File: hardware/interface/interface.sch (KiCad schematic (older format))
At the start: 14 parts, among them IC1 ARDUINO NANO, J8 CONN_01X02, Q1 BC547

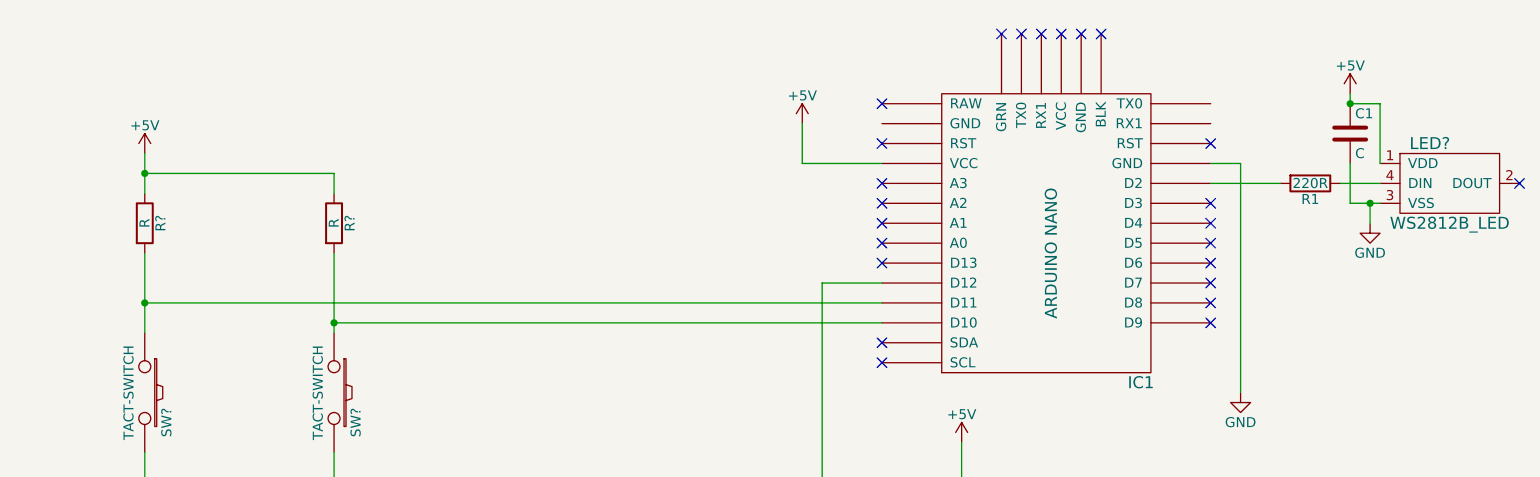
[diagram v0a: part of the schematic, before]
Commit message: Update diagram with LCD instead of LED.
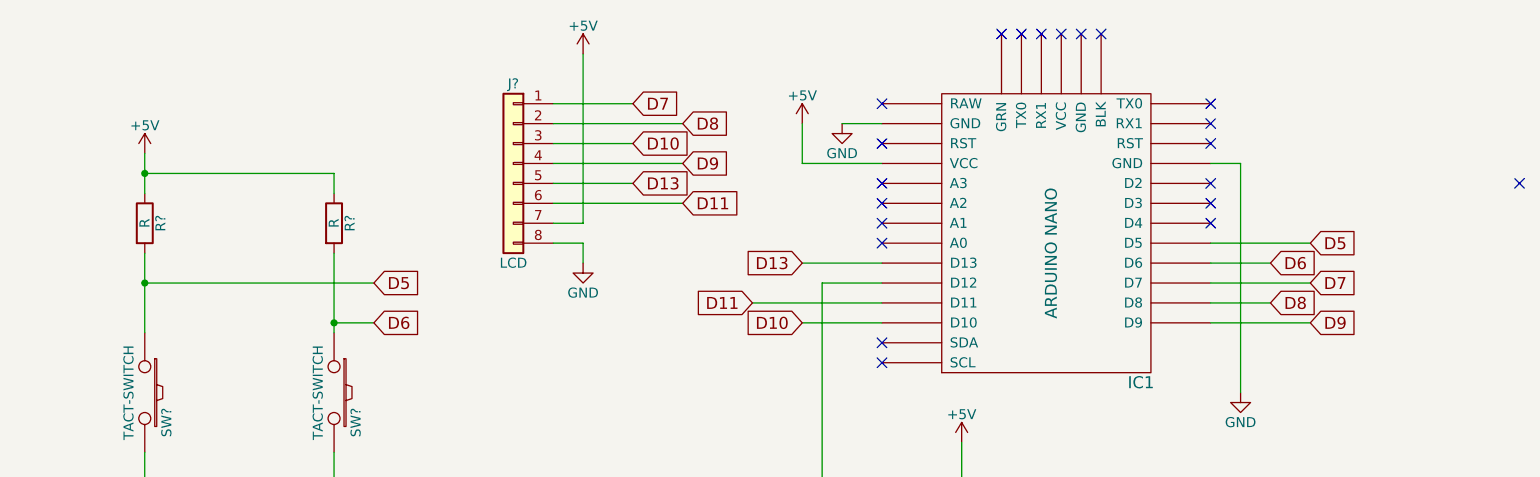
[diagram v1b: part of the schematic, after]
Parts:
- removed C1: C, symbol C
- removed LED?: WS2812B_LED, symbol WS2812B_LED
- removed R1: 220R, symbol R
- added J?: LCD, symbol Conn_01x08
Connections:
- net +5V: now also J?.7 (Pin_7)
- net GND: now also J?.8 (Pin_8)
- net D5: now reaches IC1.~ (VCC), R?.2, SW?.1
- net D6: now reaches IC1.~ (VCC), R?.2, SW?.1
- new net D10: IC1.~ (VCC), J?.3 (Pin_3)
- new net D11: IC1.~ (VCC), J?.6 (Pin_6)
- new net D13: IC1.~ (VCC), J?.5 (Pin_5)
- new net D7: IC1.~ (VCC), J?.1 (Pin_1)
- new net D8: IC1.~ (VCC), J?.2 (Pin_2)
- new net D9: IC1.~ (VCC), J?.4 (Pin_4)
- no-connect marks 24 -> 21
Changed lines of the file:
@@
 	1    0    0    -1
 $EndComp
-NoConn ~ 6650 2650
 $Comp
 L BC547 Q1
@@
 Wire Wire Line
 	1400 6350 1400 6550
-$Comp
-L WS2812B_LED LED?
-U 1 1 59806E4F
-P 9500 2250
-F 0 "LED?" H 9400 2450 60  0000 C CNN
-F 1 "WS2812B_LED" H 9500 2050 60  0000 C CNN
-F 2 "" H 9500 2250 60  0000 C CNN
-F 3 "" H 9500 2250 60  0000 C CNN
-	1    9500 2250
-	1    0    0    -1
-$EndComp
 NoConn ~ 9850 2250
-$Comp
-L R R1
-U 1 1 59806F2F
-P 8800 2250
-F 0 "R1" V 8880 2250 50  0000 C CNN
-F 1 "220R" V 8800 2250 50  0000 C CNN
-F 2 "" V 8730 2250 50  0001 C CNN
-F 3 "" H 8800 2250 50  0001 C CNN
-	1    8800 2250
-	0    1    1    0
-$EndComp
-Wire Wire Line
-	8300 2250 8650 2250
-Wire Wire Line
-	8950 2250 9150 2250
-$Comp
-L GND #PWR?
-U 1 1 59806FA3
-P 9100 2450
-F 0 "#PWR?" H 9100 2200 50  0001 C CNN
-F 1 "GND" H 9100 2300 50  0000 C CNN
-F 2 "" H 9100 2450 50  0001 C CNN
-F 3 "" H 9100 2450 50  0001 C CNN
-	1    9100 2450
-	1    0    0    -1
-$EndComp
-Wire Wire Line
-	9000 2350 9150 2350
-Wire Wire Line
-	9100 2350 9100 2450
-$Comp
-L +5V #PWR?
-U 1 1 59806FEE
-P 9000 1800
-F 0 "#PWR?" H 9000 1650 50  0001 C CNN
-F 1 "+5V" H 9000 1940 50  0000 C CNN
-F 2 "" H 9000 1800 50  0001 C CNN
-F 3 "" H 9000 1800 50  0001 C CNN
-	1    9000 1800
-	1    0    0    -1
-$EndComp
-$Comp
-L C C1
-U 1 1 59807012
-P 9000 2000
-F 0 "C1" H 9025 2100 50  0000 L CNN
-F 1 "C" H 9025 1900 50  0000 L CNN
-F 2 "" H 9038 1850 50  0001 C CNN
-F 3 "" H 9000 2000 50  0001 C CNN
-	1    9000 2000
-	1    0    0    -1
-$EndComp
-Wire Wire Line
-	9000 2150 9000 2350
-Connection ~ 9100 2350
-Wire Wire Line
-	9000 1800 9000 1850
-Wire Wire Line
-	9000 1850 9150 1850
-Wire Wire Line
-	9150 1850 9150 2150
-Connection ~ 9000 1850
 $Comp
 L TACT-SWITCH SW?
@@
 	3900 2200 3900 2300
 Connection ~ 2950 2200
-Wire Wire Line
-	6650 2850 2950 2850
-Connection ~ 2950 2850
-Wire Wire Line
-	6650 2950 3900 2950
+Connection ~ 2950 2750
 Connection ~ 3900 2950
 NoConn ~ 6650 3050
 NoConn ~ 6650 3150
+NoConn ~ 6650 2250
+NoConn ~ 6650 2350
+NoConn ~ 6650 2450
+NoConn ~ 6650 2550
+NoConn ~ 8300 2450
+NoConn ~ 8300 2350
+$Comp
+L GND #PWR?
+U 1 1 59807976
+P 8450 3300
+F 0 "#PWR?" H 8450 3050 50  0001 C CNN
+F 1 "GND" H 8450 3150 50  0000 C CNN
+F 2 "" H 8450 3300 50  0001 C CNN
+F 3 "" H 8450 3300 50  0001 C CNN
+	1    8450 3300
+	1    0    0    -1
+$EndComp
+$Comp
+L +5V #PWR?
+U 1 1 598079E4
+P 6250 1950
+F 0 "#PWR?" H 6250 1800 50  0001 C CNN
+F 1 "+5V" H 6250 2090 50  0000 C CNN
+F 2 "" H 6250 1950 50  0001 C CNN
+F 3 "" H 6250 1950 50  0001 C CNN
+	1    6250 1950
+	1    0    0    -1
+$EndComp
+Wire Wire Line
+	6250 1950 6250 2150
+Wire Wire Line
+	6250 2150 6650 2150
+Wire Wire Line
+	6650 4000 7600 4000
+$Comp
+L C C2
+U 1 1 59807C8B
+P 6650 4350
+F 0 "C2" H 6675 4450 50  0000 L CNN
+F 1 "100u" H 6675 4250 50  0000 L CNN
+F 2 "" H 6688 4200 50  0001 C CNN
+F 3 "" H 6650 4350 50  0001 C CNN
+	1    6650 4350
+	1    0    0    -1
+$EndComp
+Wire Wire Line
+	6650 4000 6650 4200
+Wire Wire Line
+	6650 4500 6650 5250
+Wire Wire Line
+	6650 5250 7600 5250
+Connection ~ 7600 5250
+$Comp
+L Conn_01x08 J?
+U 1 1 5A3D63D6
+P 4800 2150
+F 0 "J?" H 4800 2550 50  0000 C CNN
+F 1 "LCD" H 4800 1650 50  0000 C CNN
+F 2 "" H 4800 2150 50  0001 C CNN
+F 3 "" H 4800 2150 50  0001 C CNN
+	1    4800 2150
+	-1   0    0    -1
+$EndComp
+$Comp
+L GND #PWR?
+U 1 1 5A3D6483
+P 5150 2650
+F 0 "#PWR?" H 5150 2400 50  0001 C CNN
+F 1 "GND" H 5150 2500 50  0000 C CNN
+F 2 "" H 5150 2650 50  0001 C CNN
+F 3 "" H 5150 2650 50  0001 C CNN
+	1    5150 2650
+	1    0    0    -1
+$EndComp
+Wire Wire Line
+	5000 2550 5150 2550
+Wire Wire Line
+	5150 2550 5150 2650
+$Comp
+L +5V #PWR?
+U 1 1 5A3D64FD
+P 5150 1600
+F 0 "#PWR?" H 5150 1450 50  0001 C CNN
+F 1 "+5V" H 5150 1740 50  0000 C CNN
+F 2 "" H 5150 1600 50  0001 C CNN
+F 3 "" H 5150 1600 50  0001 C CNN
+	1    5150 1600
+	1    0    0    -1
+$EndComp
+Wire Wire Line
+	5150 1600 5150 2450
+Wire Wire Line
+	5150 2450 5000 2450
+Text GLabel 5650 1950 2    60   Input ~ 0
+D8
+Wire Wire Line
+	5400 1850 5000 1850
+Text GLabel 5400 2050 2    60   Input ~ 0
+D10
+Wire Wire Line
+	5650 1950 5000 1950
+Wire Wire Line
+	5400 2050 5000 2050
+Text GLabel 5650 2150 2    60   Input ~ 0
+D9
+Wire Wire Line
+	5650 2150 5000 2150
+Text GLabel 5400 2250 2    60   Input ~ 0
+D13
+Wire Wire Line
+	5400 2250 5000 2250
+Text GLabel 5650 2350 2    60   Input ~ 0
+D11
+Wire Wire Line
+	5650 2350 5000 2350
+Text GLabel 8600 2850 2    60   Input ~ 0
+D8
+Text GLabel 8800 2950 2    60   Input ~ 0
+D9
+Text GLabel 6000 2850 0    60   Input ~ 0
+D11
+Text GLabel 6250 2950 0    60   Input ~ 0
+D10
+Wire Wire Line
+	6250 2950 6650 2950
+Wire Wire Line
+	6650 2850 6000 2850
+Text GLabel 6250 2650 0    60   Input ~ 0
+D13
+Wire Wire Line
+	6250 2650 6650 2650
+Wire Wire Line
+	8300 2950 8800 2950
+Wire Wire Line
+	8600 2850 8300 2850
+Text GLabel 8800 2750 2    60   Input ~ 0
+D7
+Wire Wire Line
+	8300 2750 8800 2750
+Text GLabel 5400 1850 2    60   Input ~ 0
+D7
 $Comp
 L ARDUINO_PRO_MINI_5V IC1
@@
 	1    0    0    1
 $EndComp
-NoConn ~ 6650 2250
-NoConn ~ 6650 2350
-NoConn ~ 6650 2450
-NoConn ~ 6650 2550
-NoConn ~ 8300 2750
-NoConn ~ 8300 2650
-NoConn ~ 8300 2550
-NoConn ~ 8300 2450
-NoConn ~ 8300 2350
-NoConn ~ 8300 2850
-NoConn ~ 8300 2950
+Text GLabel 8600 2650 2    60   Input ~ 0
+D6
+Text GLabel 8800 2550 2    60   Input ~ 0
+D5
+Wire Wire Line
+	8800 2550 8300 2550
+Wire Wire Line
+	8300 2650 8600 2650
+Text GLabel 4100 2750 2    60   Input ~ 0
+D5
+Text GLabel 4100 2950 2    60   Input ~ 0
+D6
+Wire Wire Line
+	4100 2950 3900 2950
+Wire Wire Line
+	4100 2750 2950 2750
+NoConn ~ 8300 1950
+NoConn ~ 8300 1850
+NoConn ~ 8300 2250
 $Comp
 L GND #PWR?
-U 1 1 59807976
-P 8450 3300
-F 0 "#PWR?" H 8450 3050 50  0001 C CNN
-F 1 "GND" H 8450 3150 50  0000 C CNN
-F 2 "" H 8450 3300 50  0001 C CNN
-F 3 "" H 8450 3300 50  0001 C CNN
-	1    8450 3300
-	1    0    0    -1
-$EndComp
-$Comp
-L +5V #PWR?
-U 1 1 598079E4
-P 6250 1950
-F 0 "#PWR?" H 6250 1800 50  0001 C CNN
-F 1 "+5V" H 6250 2090 50  0000 C CNN
-F 2 "" H 6250 1950 50  0001 C CNN
-F 3 "" H 6250 1950 50  0001 C CNN
-	1    6250 1950
-	1    0    0    -1
-$EndComp
-Wire Wire Line
-	6250 1950 6250 2150
-Wire Wire Line
-	6250 2150 6650 2150
-Wire Wire Line
-	6650 4000 7600 4000
-$Comp
-L C C2
-U 1 1 59807C8B
-P 6650 4350
-F 0 "C2" H 6675 4450 50  0000 L CNN
-F 1 "100u" H 6675 4250 50  0000 L CNN
-F 2 "" H 6688 4200 50  0001 C CNN
-F 3 "" H 6650 4350 50  0001 C CNN
-	1    6650 4350
-	1    0    0    -1
-$EndComp
-Wire Wire Line
-	6650 4000 6650 4200
-Wire Wire Line
-	6650 4500 6650 5250
-Wire Wire Line
-	6650 5250 7600 5250
-Connection ~ 7600 5250
+U 1 1 5A3D73AC
+P 6450 1950
+F 0 "#PWR?" H 6450 1700 50  0001 C CNN
+F 1 "GND" H 6450 1800 50  0000 C CNN
+F 2 "" H 6450 1950 50  0001 C CNN
+F 3 "" H 6450 1950 50  0001 C CNN
+	1    6450 1950
+	1    0    0    -1
+$EndComp
+Wire Wire Line
+	6450 1950 6650 1950
 $EndSCHEMATC
